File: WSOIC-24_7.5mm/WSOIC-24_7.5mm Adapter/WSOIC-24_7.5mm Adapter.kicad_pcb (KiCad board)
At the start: 2 copper layers, 20.3 x 30.5 mm, 3 parts, among them J1 Conn_01x12_Male, J2 Conn_01x12_Male, U1 24-Pin_Chip

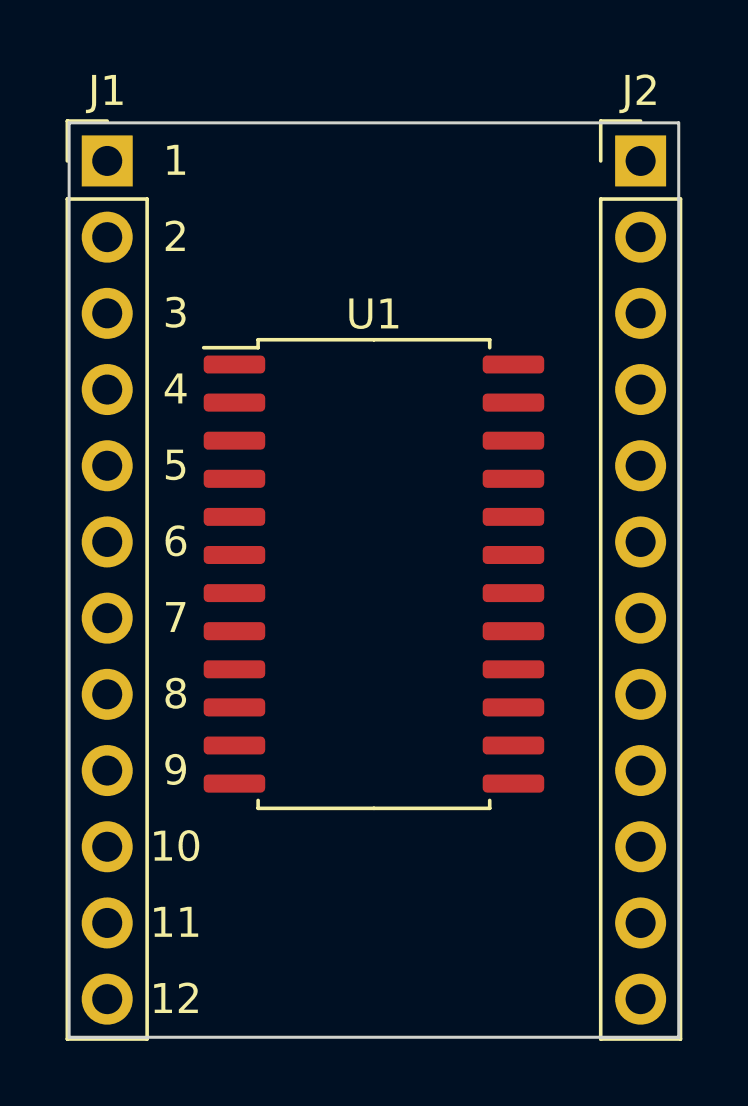
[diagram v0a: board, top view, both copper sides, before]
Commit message: WSOIC-24 PCB routed and silkscreen finished
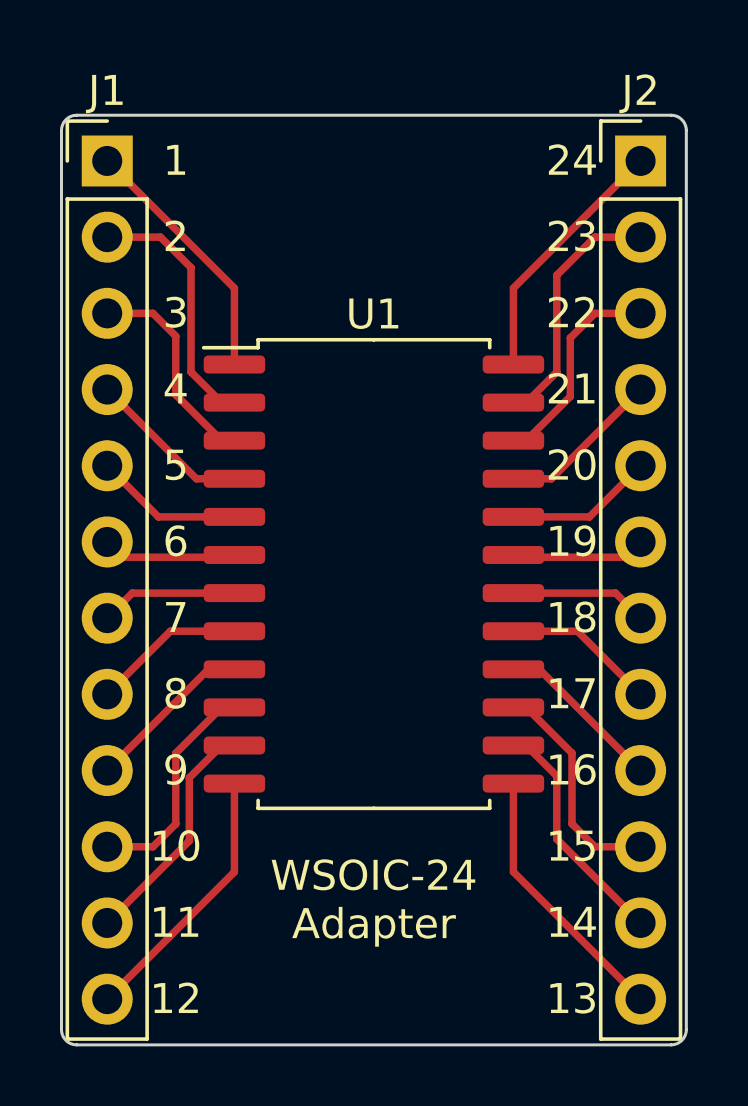
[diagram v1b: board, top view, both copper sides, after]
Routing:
- net Net-(U1-Pad13): track 0.00 -> 8.94 mm
- net Net-(J1-Pad12): track 0.00 -> 8.94 mm
- net Net-(J1-Pad2): track 0.00 -> 8.56 mm
- net Net-(J2-Pad1): track 0.00 -> 8.54 mm
- net Net-(J1-Pad1): track 0.00 -> 8.54 mm
- net Net-(J2-Pad2): track 0.00 -> 8.41 mm
- net Net-(U1-Pad14): track 0.00 -> 7.92 mm
- net Net-(J1-Pad11): track 0.00 -> 7.92 mm
- net Net-(U1-Pad15): track 0.00 -> 7.54 mm
- net Net-(J1-Pad10): track 0.00 -> 7.54 mm
- net Net-(U1-Pad22): track 0.00 -> 7.14 mm
- net Net-(J1-Pad3): track 0.00 -> 7.14 mm
- net Net-(U1-Pad16): track 0.00 -> 5.64 mm
- net Net-(J1-Pad9): track 0.00 -> 5.64 mm
- net Net-(U1-Pad21): track 0.00 -> 5.47 mm
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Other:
- board size 20.3 x 30.5 mm -> 20.8 x 31 mm
- board text added: "13"
- board text added: "14"
- board text added: "15"
- board text added: "16"
- board text added: "17"
- board text added: "18"
- board text added: "19"
- board text added: "20"
- board text added: "21"
- board text added: "22"
- board text added: "23"
- board text added: "24"
- board text added: "WSOIC-24 Adapter"
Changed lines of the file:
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@@
     )
   )
-  (gr_rect (start 128.27 110.49) (end 107.95 80.01) (layer "Edge.Cuts") (width 0.1) (fill none))
+  (gr_arc (start 107.696 80.264) (mid 107.84479 79.90479) (end 108.204 79.756) (layer "Edge.Cuts") (width 0.1))
+  (gr_arc (start 128.016 79.756) (mid 128.37521 79.90479) (end 128.524 80.264) (layer "Edge.Cuts") (width 0.1))
+  (gr_line (start 128.524 110.236) (end 128.524 80.264) (layer "Edge.Cuts") (width 0.1))
+  (gr_arc (start 108.204 110.744) (mid 107.84479 110.59521) (end 107.696 110.236) (layer "Edge.Cuts") (width 0.1))
+  (gr_arc (start 128.524 110.236) (mid 128.37521 110.59521) (end 128.016 110.744) (layer "Edge.Cuts") (width 0.1))
+  (gr_line (start 108.204 110.744) (end 128.016 110.744) (layer "Edge.Cuts") (width 0.1))
+  (gr_line (start 107.696 80.264) (end 107.696 110.236) (layer "Edge.Cuts") (width 0.1))
+  (gr_line (start 128.016 79.756) (end 108.204 79.756) (layer "Edge.Cuts") (width 0.1))
+  (gr_text "24" (at 124.714 81.28) (layer "F.SilkS")
+    (effects (font (size 1 1) (thickness 0.15)))
+  )
+  (gr_text "WSOIC-24\nAdapter" (at 118.11 105.918) (layer "F.SilkS")
+    (effects (font (size 1 1) (thickness 0.15)))
+  )
   (gr_text "12" (at 111.506 109.22) (layer "F.SilkS")
     (effects (font (size 1 1) (thickness 0.15)))
   )
+  (gr_text "19" (at 124.714 93.98) (layer "F.SilkS")
+    (effects (font (size 1 1) (thickness 0.15)))
+  )
   (gr_text "10" (at 111.506 104.14) (layer "F.SilkS")
+    (effects (font (size 1 1) (thickness 0.15)))
+  )
+  (gr_text "13" (at 124.714 109.22) (layer "F.SilkS")
     (effects (font (size 1 1) (thickness 0.15)))
   )
@@
   )
   (gr_text "11" (at 111.506 106.68) (layer "F.SilkS")
+    (effects (font (size 1 1) (thickness 0.15)))
+  )
+  (gr_text "23" (at 124.714 83.82) (layer "F.SilkS")
+    (effects (font (size 1 1) (thickness 0.15)))
+  )
+  (gr_text "22" (at 124.714 86.36) (layer "F.SilkS")
     (effects (font (size 1 1) (thickness 0.15)))
   )
@@
     (effects (font (size 1 1) (thickness 0.15)))
   )
+  (gr_text "18" (at 124.714 96.52) (layer "F.SilkS")
+    (effects (font (size 1 1) (thickness 0.15)))
+  )
   (gr_text "6" (at 111.506 93.98) (layer "F.SilkS")
+    (effects (font (size 1 1) (thickness 0.15)))
+  )
+  (gr_text "21" (at 124.714 88.9) (layer "F.SilkS")
+    (effects (font (size 1 1) (thickness 0.15)))
+  )
+  (gr_text "16" (at 124.714 101.6) (layer "F.SilkS")
     (effects (font (size 1 1) (thickness 0.15)))
   )
@@
     (effects (font (size 1 1) (thickness 0.15)))
   )
+  (gr_text "15" (at 124.714 104.14) (layer "F.SilkS")
+    (effects (font (size 1 1) (thickness 0.15)))
+  )
+  (gr_text "14" (at 124.714 106.68) (layer "F.SilkS")
+    (effects (font (size 1 1) (thickness 0.15)))
+  )
+  (gr_text "17" (at 124.714 99.06) (layer "F.SilkS")
+    (effects (font (size 1 1) (thickness 0.15)))
+  )
+  (gr_text "20" (at 124.714 91.44) (layer "F.SilkS")
+    (effects (font (size 1 1) (thickness 0.15)))
+  )
+  (segment (start 113.46 88.065) (end 113.46 85.52) (width 0.25) (layer "F.Cu") (net 1))
+  (segment (start 113.46 85.52) (end 109.22 81.28) (width 0.25) (layer "F.Cu") (net 1))
+  (segment (start 113.46 89.335) (end 113.033928 89.335) (width 0.25) (layer "F.Cu") (net 2))
+  (segment (start 112.014 84.836) (end 110.998 83.82) (width 0.25) (layer "F.Cu") (net 2))
+  (segment (start 113.033928 89.335) (end 112.014 88.315072) (width 0.25) (layer "F.Cu") (net 2))
+  (segment (start 112.014 88.315072) (end 112.014 84.836) (width 0.25) (layer "F.Cu") (net 2))
+  (segment (start 110.998 83.82) (end 109.22 83.82) (width 0.25) (layer "F.Cu") (net 2))
+  (segment (start 110.744 86.36) (end 109.22 86.36) (width 0.25) (layer "F.Cu") (net 3))
+  (segment (start 111.506 87.122) (end 110.744 86.36) (width 0.25) (layer "F.Cu") (net 3))
+  (segment (start 113.46 90.605) (end 113.033928 90.605) (width 0.25) (layer "F.Cu") (net 3))
+  (segment (start 113.033928 90.605) (end 111.506 89.077072) (width 0.25) (layer "F.Cu") (net 3))
+  (segment (start 111.506 89.077072) (end 111.506 87.122) (width 0.25) (layer "F.Cu") (net 3))
+  (segment (start 113.46 91.875) (end 112.195 91.875) (width 0.25) (layer "F.Cu") (net 4))
+  (segment (start 112.195 91.875) (end 109.22 88.9) (width 0.25) (layer "F.Cu") (net 4))
+  (segment (start 113.46 93.145) (end 110.925 93.145) (width 0.25) (layer "F.Cu") (net 5))
+  (segment (start 110.925 93.145) (end 109.22 91.44) (width 0.25) (layer "F.Cu") (net 5))
+  (segment (start 109.728 94.488) (end 109.22 93.98) (width 0.25) (layer "F.Cu") (net 6))
+  (segment (start 113.46 94.415) (end 113.387 94.488) (width 0.25) (layer "F.Cu") (net 6))
+  (segment (start 113.387 94.488) (end 109.728 94.488) (width 0.25) (layer "F.Cu") (net 6))
+  (segment (start 113.46 95.685) (end 110.055 95.685) (width 0.25) (layer "F.Cu") (net 7))
+  (segment (start 110.055 95.685) (end 109.22 96.52) (width 0.25) (layer "F.Cu") (net 7))
+  (segment (start 113.46 96.955) (end 111.325 96.955) (width 0.25) (layer "F.Cu") (net 8))
+  (segment (start 111.325 96.955) (end 109.22 99.06) (width 0.25) (layer "F.Cu") (net 8))
+  (segment (start 112.595 98.225) (end 109.22 101.6) (width 0.25) (layer "F.Cu") (net 9))
+  (segment (start 113.46 98.225) (end 112.595 98.225) (width 0.25) (layer "F.Cu") (net 9))
+  (segment (start 111.506 103.378) (end 110.744 104.14) (width 0.25) (layer "F.Cu") (net 10))
+  (segment (start 113.46 99.495) (end 113.033928 99.495) (width 0.25) (layer "F.Cu") (net 10))
+  (segment (start 110.744 104.14) (end 109.22 104.14) (width 0.25) (layer "F.Cu") (net 10))
+  (segment (start 111.506 101.022928) (end 111.506 103.378) (width 0.25) (layer "F.Cu") (net 10))
+  (segment (start 113.033928 99.495) (end 111.506 101.022928) (width 0.25) (layer "F.Cu") (net 10))
+  (segment (start 113.46 100.765) (end 113.033928 100.765) (width 0.25) (layer "F.Cu") (net 11))
+  (segment (start 111.95552 101.843408) (end 111.95552 103.94448) (width 0.25) (layer "F.Cu") (net 11))
+  (segment (start 111.95552 103.94448) (end 109.22 106.68) (width 0.25) (layer "F.Cu") (net 11))
+  (segment (start 113.033928 100.765) (end 111.95552 101.843408) (width 0.25) (layer "F.Cu") (net 11))
+  (segment (start 113.46 104.98) (end 109.22 109.22) (width 0.25) (layer "F.Cu") (net 12))
+  (segment (start 113.46 102.035) (end 113.46 104.98) (width 0.25) (layer "F.Cu") (net 12))
+  (segment (start 122.76 88.065) (end 122.76 85.52) (width 0.25) (layer "F.Cu") (net 13))
+  (segment (start 122.76 85.52) (end 127 81.28) (width 0.25) (layer "F.Cu") (net 13))
+  (segment (start 124.206 85.09) (end 125.476 83.82) (width 0.25) (layer "F.Cu") (net 14))
+  (segment (start 124.206 88.315072) (end 124.206 85.09) (width 0.25) (layer "F.Cu") (net 14))
+  (segment (start 123.186072 89.335) (end 124.206 88.315072) (width 0.25) (layer "F.Cu") (net 14))
+  (segment (start 122.76 89.335) (end 123.186072 89.335) (width 0.25) (layer "F.Cu") (net 14))
+  (segment (start 125.476 83.82) (end 127 83.82) (width 0.25) (layer "F.Cu") (net 14))
+  (segment (start 124.65552 89.135552) (end 124.65552 87.18048) (width 0.25) (layer "F.Cu") (net 15))
+  (segment (start 123.186072 90.605) (end 124.65552 89.135552) (width 0.25) (layer "F.Cu") (net 15))
+  (segment (start 122.76 90.605) (end 123.186072 90.605) (width 0.25) (layer "F.Cu") (net 15))
+  (segment (start 124.65552 87.18048) (end 125.476 86.36) (width 0.25) (layer "F.Cu") (net 15))
+  (segment (start 125.476 86.36) (end 127 86.36) (width 0.25) (layer "F.Cu") (net 15))
+  (segment (start 122.76 91.875) (end 124.025 91.875) (width 0.25) (layer "F.Cu") (net 16))
+  (segment (start 124.025 91.875) (end 127 88.9) (width 0.25) (layer "F.Cu") (net 16))
+  (segment (start 122.76 93.145) (end 125.295 93.145) (width 0.25) (layer "F.Cu") (net 17))
+  (segment (start 125.295 93.145) (end 127 91.44) (width 0.25) (layer "F.Cu") (net 17))
+  (segment (start 126.492 94.488) (end 127 93.98) (width 0.25) (layer "F.Cu") (net 18))
+  (segment (start 122.76 94.415) (end 122.833 94.488) (width 0.25) (layer "F.Cu") (net 18))
+  (segment (start 122.833 94.488) (end 126.492 94.488) (width 0.25) (layer "F.Cu") (net 18))
+  (segment (start 126.165 95.685) (end 127 96.52) (width 0.25) (layer "F.Cu") (net 19))
+  (segment (start 122.76 95.685) (end 126.165 95.685) (width 0.25) (layer "F.Cu") (net 19))
+  (segment (start 122.76 96.955) (end 124.895 96.955) (width 0.25) (layer "F.Cu") (net 20))
+  (segment (start 124.895 96.955) (end 127 99.06) (width 0.25) (layer "F.Cu") (net 20))
+  (segment (start 123.625 98.225) (end 127 101.6) (width 0.25) (layer "F.Cu") (net 21))
+  (segment (start 122.76 98.225) (end 123.625 98.225) (width 0.25) (layer "F.Cu") (net 21))
+  (segment (start 124.714 103.378) (end 125.476 104.14) (width 0.25) (layer "F.Cu") (net 22))
+  (segment (start 122.76 99.495) (end 123.186072 99.495) (width 0.25) (layer "F.Cu") (net 22))
+  (segment (start 124.714 101.022928) (end 124.714 103.378) (width 0.25) (layer "F.Cu") (net 22))
+  (segment (start 123.186072 99.495) (end 124.714 101.022928) (width 0.25) (layer "F.Cu") (net 22))
+  (segment (start 125.476 104.14) (end 127 104.14) (width 0.25) (layer "F.Cu") (net 22))
+  (segment (start 124.206 101.784928) (end 124.206 103.886) (width 0.25) (layer "F.Cu") (net 23))
+  (segment (start 124.206 103.886) (end 127 106.68) (width 0.25) (layer "F.Cu") (net 23))
+  (segment (start 123.186072 100.765) (end 124.206 101.784928) (width 0.25) (layer "F.Cu") (net 23))
+  (segment (start 122.76 100.765) (end 123.186072 100.765) (width 0.25) (layer "F.Cu") (net 23))
+  (segment (start 122.76 102.035) (end 122.76 104.98) (width 0.25) (layer "F.Cu") (net 24))
+  (segment (start 122.76 104.98) (end 127 109.22) (width 0.25) (layer "F.Cu") (net 24))
 )
